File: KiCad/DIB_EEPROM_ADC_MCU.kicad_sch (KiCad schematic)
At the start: 59 parts, among them IC1 ISO6762FDWR, IC2 ISO6762FDWR, IC3 ADS131M04IPWR, IC4 STM32H503CBT6, IC5 M24C32-DFDW6TP, X1 Edge connector, X2 N.C., Y1 FD0810004, Y2 ABM8-25.000MHZ-D2X-T

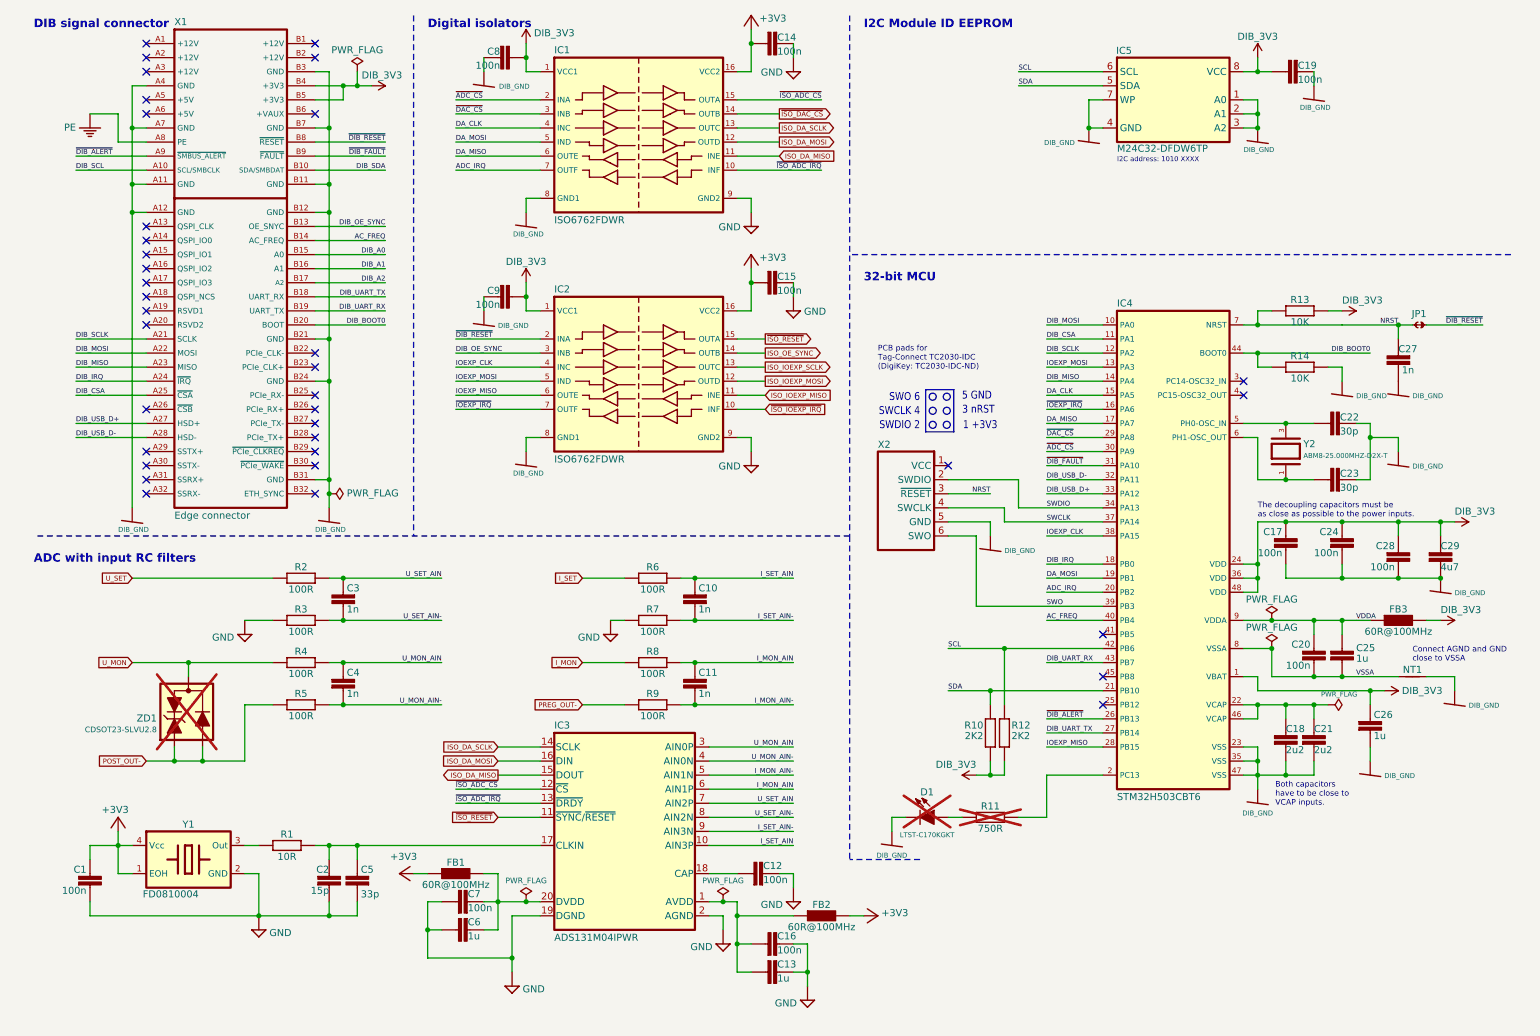
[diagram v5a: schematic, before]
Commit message: r4B4 (ADC replaced with ADS131A04)
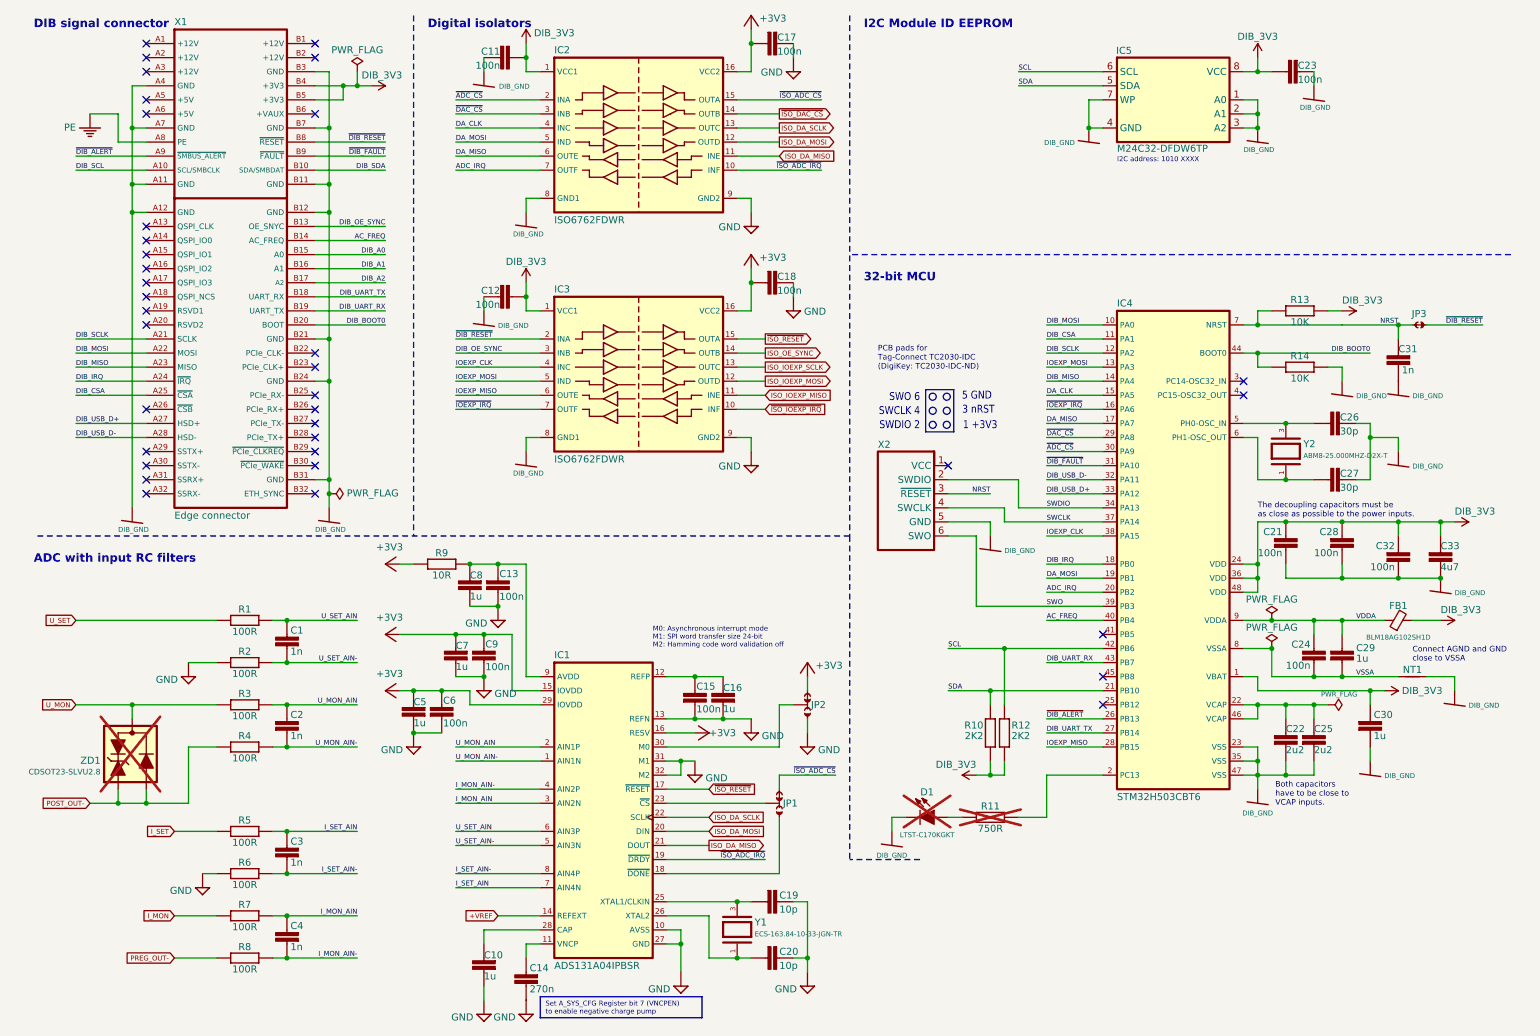
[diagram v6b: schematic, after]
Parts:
- removed C1, C12: 100n, PCM_EEZ_passives:C_0603_1608Metric, symbol PCM_EEZ_passives:C-EU
- removed C2: 15p, PCM_EEZ_passives:C_0603_1608Metric, symbol PCM_EEZ_passives:C-EU
- removed FB1, FB2: 60R@100MHz, PCM_EEZ_passives:BEAD0603, symbol PCM_EEZ_passives:L_EU
- removed IC3: ADS131M04IPWR, PCM_EEZ_SMD:TSSOP-20, symbol PCM_EEZ_TI:ADS131M04IPWR
- removed R1: 10R, PCM_EEZ_passives:R_0805_2012Metric, symbol PCM_EEZ_passives:R-EU
- removed Y1: FD0810004, PCM_EEZ_passives:FD081_DIO-L, symbol PCM_EEZ_passives:XTAL OSC (4-pins)
- added C10, C8: 1u, PCM_EEZ_passives:C_0805_2012Metric, symbol PCM_EEZ_passives:C-EU
- added C14: 270n, PCM_EEZ_passives:C_0603_1608Metric, symbol PCM_EEZ_passives:C-EU
- added C15, C9: 100n, PCM_EEZ_passives:C_0603_1608Metric, symbol PCM_EEZ_passives:C-EU
- added C19, C20: 10p, PCM_EEZ_passives:C_0603_1608Metric, symbol PCM_EEZ_passives:C-EU
- added IC1: ADS131A04IPBSR, PCM_EEZ_SMD:QFP50P700X700X120-32N, symbol PCM_EEZ_TI:ADS131A04IPBSR
- added JP1, JP2: 0R, PCM_EEZ_SMD:JP3 shorted (0603), symbol PCM_EEZ_unsorted:JP3 shorted
- added R9: 10R, PCM_EEZ_passives:R_0805_2012Metric, symbol PCM_EEZ_passives:R-EU
- added Y1: ECS-163.84-10-33-JGN-TR, PCM_EEZ_passives:XTAL_403C11A24M00000, symbol PCM_EEZ_passives:XTAL (LFXTAL026392)
- C13, C6: value 1u -> 100n; footprint PCM_EEZ_passives:C_0805_2012Metric -> PCM_EEZ_passives:C_0603_1608Metric; DigiKey 587-1283-1-ND -> 490-4774-1-ND; Mouser 603-CC805MKX7R7BB105 -> 80-C0603C104M4R; TME CL21B105KOFNNNE -> CL10B104KA8NNNC
- C16, C7: value 100n -> 1u; footprint PCM_EEZ_passives:C_0603_1608Metric -> PCM_EEZ_passives:C_0805_2012Metric; DigiKey 490-4774-1-ND -> 587-1283-1-ND; Mouser 80-C0603C104M4R -> 603-CC805MKX7R7BB105; TME CL10B104KA8NNNC -> CL21B105KOFNNNE
- C5: value 33p -> 1u; DigiKey 1276-1105-1-ND -> 587-1283-1-ND; Mouser C0805C330K5GACTU -> 603-CC805MKX7R7BB105; TME CL21C330JBANNNC -> CL21B105KOFNNNE
- FB1: renamed from FB3; value 60R@100MHz -> BLM18AG102SH1D; symbol PCM_EEZ_passives:L_EU -> PCM_EEZ_passives:L_Ferrite Bead
- renumbered C3 to C1, C8 to C11, C9 to C12, C14 to C17, C15 to C18, C4 to C2, C17 to C21, C18 to C22, C19 to C23, C20 to C24, C21 to C25, C22 to C26, C23 to C27, C24 to C28, C25 to C29, C10 to C3, C26 to C30, C27 to C31, C28 to C32, C29 to C33, C11 to C4, IC1 to IC2, IC2 to IC3, JP1 to JP3, R2 to R1, R3 to R2, R4 to R3, R5 to R4, R6 to R5, R7 to R6, R8 to R7, R9 to R8
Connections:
- net +3V3: now also C5.1, C6.2, C7.1, C9.2, IC1.15 (IOVDD), IC1.16 (RESV), IC1.29 (IOVDD), JP2.NC, R9.1
- net GND: now also C13.1, C16.2, C10.2, C14.1, C15.1, C19.1, C20.1, C8.2, C9.1, IC1.10 (AVSS), IC1.13 (REFN), IC1.27 (GND), IC1.31 (M1), IC1.32 (M2), JP2.NO; no longer C13.2, C16.1
- net ISO_DA_MISO: now also IC1.21 (DOUT)
- net ISO_DA_MOSI: now also IC1.20 (DIN)
- net ISO_DA_SCLK: now also IC1.22 (SCLK)
- net I_MON_AIN: now also IC1.3 (AIN2N)
- net I_MON_AIN-: now also IC1.4 (AIN2P)
- net I_SET_AIN: now also IC1.7 (AIN4N)
- net I_SET_AIN-: now also IC1.8 (AIN4P)
- net U_MON_AIN: now also IC1.2 (AIN1P)
- net U_MON_AIN-: now also IC1.1 (AIN1N)
- net U_SET_AIN: now also IC1.6 (AIN3P)
- net U_SET_AIN-: now also IC1.5 (AIN3N)
- net ~{ISO_ADC_CS}: now also JP1.NC
- net ~{ISO_ADC_IRQ}: now also IC1.19 (~{DRDY})
- net ~{ISO_RESET}: now also IC1.17 (~{RESET})
- new net: C13.2, C8.1, IC1.9 (AVDD), R9.2
- new net: C14.2, IC1.11 (VNCP)
- new net: C15.2, C16.1, IC1.12 (REFP)
- new net: IC1.18 (~{DONE}), JP1.NO
- new net: IC1.23 (~{CS}), JP1.COM
- new net: C19.2, IC1.25 (XTAL1/CLKIN), Y1.3
- new net: C20.2, IC1.26 (XTAL2), Y1.1
- new net: C10.1, IC1.28 (CAP)
- new net: IC1.30 (M0), JP2.COM
- new net +VREF: IC1.14 (REFEXT)
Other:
- note added: "M0: Asynchronous interrupt mode M1: SPI word transfer size 24-bit M2: Hamming code word validation off"
- moved on the sheet: C1, C2, C3, C4, R1, R2, R3, R4, R5, R6, R7, R8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

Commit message: SPI channels renamed
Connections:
- net ISO_DA_MISO renamed ISO_MISO2
- net ISO_DA_MOSI renamed ISO_MOSI2
- net ISO_DA_SCLK renamed ISO_SCLK2
- net ISO_IOEXP_MISO renamed ISO_MISO1
- net ISO_IOEXP_MOSI renamed ISO_MOSI1
- net ISO_IOEXP_SCLK renamed ISO_SCLK1
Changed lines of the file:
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@@
 		)
 	)
-	(global_label "ISO_DA_MOSI"
+	(global_label "ISO_MOSI2"
 		(shape input)
 		(at 137.16 162.56 0)
@@
 		)
 	)
-	(global_label "ISO_DA_MOSI"
+	(global_label "ISO_MOSI2"
 		(shape output)
 		(at 149.86 38.1 0)
@@
 		)
 	)
-	(global_label "ISO_IOEXP_MOSI"
+	(global_label "ISO_MOSI1"
 		(shape output)
 		(at 147.32 81.28 0)
@@
 		)
 	)
-	(global_label "ISO_DA_MISO"
+	(global_label "ISO_MISO2"
 		(shape input)
 		(at 149.86 40.64 0)
@@
 		)
 	)
-	(global_label "ISO_DA_MISO"
+	(global_label "ISO_MISO2"
 		(shape output)
 		(at 137.16 165.1 0)
@@
 		)
 	)
-	(global_label "ISO_IOEXP_MISO"
+	(global_label "ISO_MISO1"
 		(shape input)
 		(at 147.32 83.82 0)
@@
 		)
 	)
-	(global_label "ISO_DA_SCLK"
+	(global_label "ISO_SCLK2"
 		(shape output)
 		(at 149.86 35.56 0)
@@
 		)
 	)
-	(global_label "ISO_IOEXP_SCLK"
+	(global_label "ISO_SCLK1"
 		(shape output)
 		(at 147.32 78.74 0)
@@
 		)
 		(property "Intersheetrefs" "${INTERSHEET_REFS}"
-			(at 160.2044 78.74 0)
+			(at 156.4792 78.74 0)
 			(effects
 				(font
@@
 		)
 	)
-	(global_label "ISO_DA_SCLK"
+	(global_label "ISO_SCLK2"
 		(shape input)
 		(at 137.16 160.02 0)

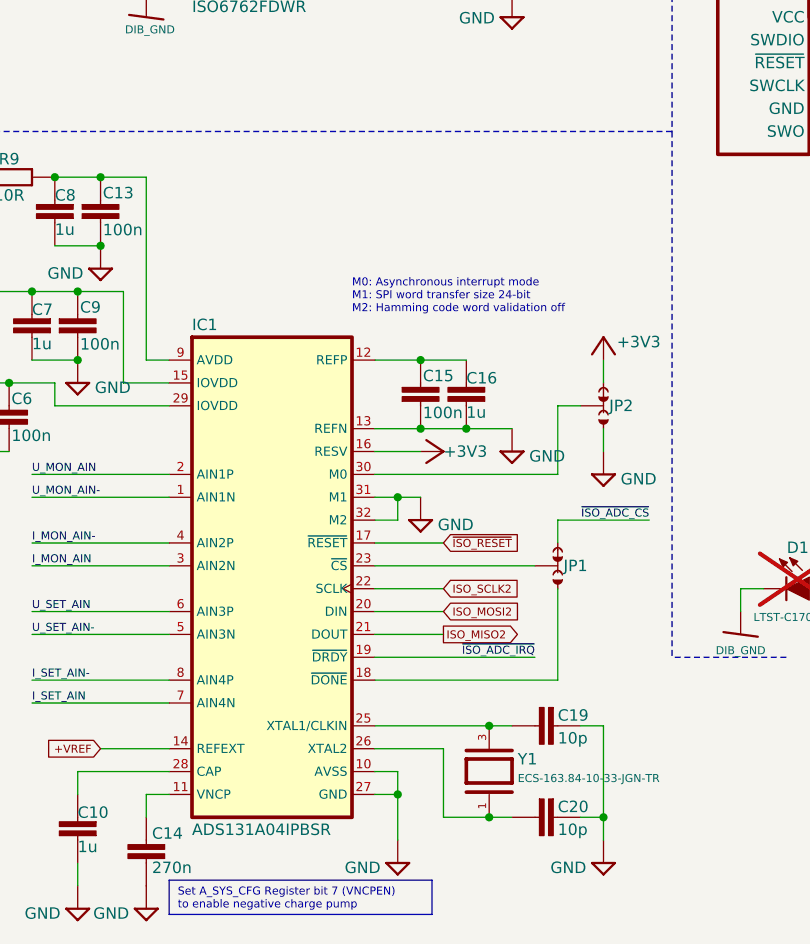
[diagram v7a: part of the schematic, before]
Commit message: Move DAC to SPI channel 1
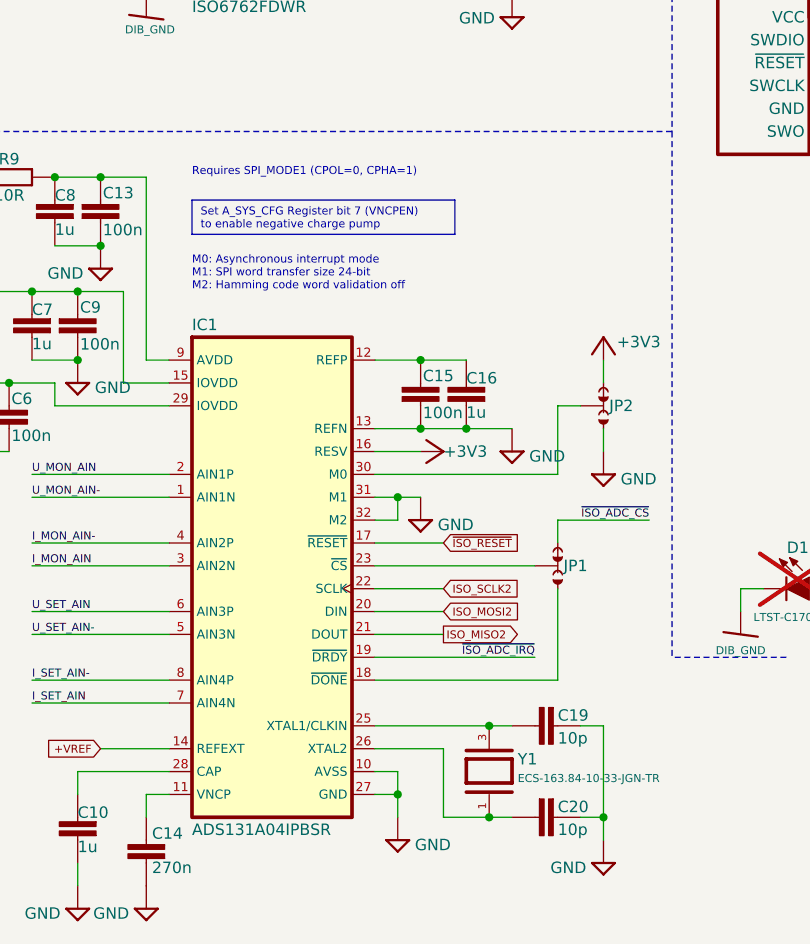
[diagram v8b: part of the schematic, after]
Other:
- note added: "Requires SPI_MODE1 (CPOL=0, CPHA=1)"
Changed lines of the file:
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@@
 		)
 	)
+	(text "Requires SPI_MODE1 (CPOL=0, CPHA=1)"
+		(exclude_from_sim no)
+		(at 109.22 114.3 0)
+		(effects
+			(font
+				(size 0.889 0.889)
+				(color 132 0 132 1)
+			)
+			(justify left bottom)
+		)
+	)
 	(text "DIB signal connector"
 		(exclude_from_sim no)
@@
 	(text "M0: Asynchronous interrupt mode\nM1: SPI word transfer size 24-bit\nM2: Hamming code word validation off"
 		(exclude_from_sim no)
-		(at 127 129.54 0)
+		(at 109.22 127 0)
 		(effects
 			(font
@@
 	(text_box "Set A_SYS_CFG Register bit 7 (VNCPEN) to enable negative charge pump"
 		(exclude_from_sim no)
-		(at 106.68 192.405 0)
+		(at 109.22 116.84 0)
 		(size 29.21 3.81)
 		(margins 0.9525 0.9525 0.9525 0.9525)
@@
 	(wire
 		(pts
-			(xy 132.08 182.88) (xy 132.08 187.96)
+			(xy 132.08 182.88) (xy 132.08 185.42)
 		)
 		(stroke
@@
 	(symbol
 		(lib_id "PCM_EEZ_symbols:GND")
-		(at 132.08 190.5 0)
-		(mirror y)
+		(at 132.08 187.96 0)
 		(unit 1)
 		(exclude_from_sim no)
@@
 		(dnp no)
 		(property "Reference" "#SUPPLY08"
-			(at 132.08 190.5 0)
+			(at 132.08 187.96 0)
 			(effects
 				(font
@@
 		)
 		(property "Value" "GND"
-			(at 130.175 191.77 0)
+			(at 133.985 189.23 0)
 			(effects
 				(font
@@
 		)
 		(property "Footprint" ""
-			(at 132.08 190.5 0)
+			(at 132.08 187.96 0)
 			(effects
 				(font
@@
 		)
 		(property "Datasheet" ""
-			(at 132.08 190.5 0)
+			(at 132.08 187.96 0)
 			(effects
 				(font
@@
 		)
 		(property "Description" ""
-			(at 132.08 190.5 0)
+			(at 132.08 187.96 0)
 			(effects
 				(font
